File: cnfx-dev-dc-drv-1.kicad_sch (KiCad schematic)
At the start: 55 parts, among them J1 TC2030, J2 Conn_01x02, J3 Conn_01x04_Pin, J4 Conn_01x02, J7 Conn_01x03, J8 Conn_01x04_Pin, SW1 SW_Push, SW2 SW_Push, SW3 SW_Push, U1 SN65HVD230, U2 STM32F103C8Tx, U5 HT753-1, U6 TPS259472A, Y1 8M

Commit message: schem: run and fix ERC
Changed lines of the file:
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@@
 	)
 	(junction
+		(at 26.67 157.48)
+		(diameter 0)
+		(color 0 0 0 0)
+	)
+	(junction
 		(at 173.99 44.45)
 		(diameter 0)
@@
 	)
 	(junction
+		(at 25.4 153.67)
+		(diameter 0)
+		(color 0 0 0 0)
+	)
+	(junction
 		(at 62.23 124.46)
 		(diameter 0)
@@
 	(wire
 		(pts
-			(xy 24.13 153.67) (xy 27.94 153.67)
+			(xy 24.13 153.67) (xy 25.4 153.67)
 		)
 		(stroke
@@
 	(wire
 		(pts
+			(xy 25.4 153.67) (xy 27.94 153.67)
+		)
+		(stroke
+			(width 0)
+			(type default)
+		)
+	)
+	(wire
+		(pts
 			(xy 165.1 53.34) (xy 165.1 54.61)
 		)
@@
 	(wire
 		(pts
-			(xy 26.67 158.75) (xy 26.67 156.21)
+			(xy 26.67 158.75) (xy 26.67 157.48)
 		)
 		(stroke
@@
 	(wire
 		(pts
+			(xy 26.67 157.48) (xy 26.67 156.21)
+		)
+		(stroke
+			(width 0)
+			(type default)
+		)
+	)
+	(wire
+		(pts
 			(xy 35.56 166.37) (xy 36.83 166.37)
 		)
@@
 	)
 	(symbol
+		(lib_id "power:PWR_FLAG")
+		(at 26.67 157.48 270)
+		(unit 1)
+		(body_style 1)
+		(exclude_from_sim no)
+		(in_bom yes)
+		(on_board yes)
+		(in_pos_files yes)
+		(dnp no)
+		(fields_autoplaced yes)
+		(property "Reference" "#FLG02"
+			(at 28.575 157.48 0)
+			(hide yes)
+			(show_name no)
+			(do_not_autoplace no)
+			(effects
+				(font
+					(size 1.27 1.27)
+				)
+			)
+		)
+		(property "Value" "PWR_FLAG"
+			(at 31.75 157.48 0)
+			(hide yes)
+			(show_name no)
+			(do_not_autoplace no)
+			(effects
+				(font
+					(size 1.27 1.27)
+				)
+			)
+		)
+		(property "Footprint" ""
+			(at 26.67 157.48 0)
+			(hide yes)
+			(show_name no)
+			(do_not_autoplace no)
+			(effects
+				(font
+					(size 1.27 1.27)
+				)
+			)
+		)
+		(property "Datasheet" ""
+			(at 26.67 157.48 0)
+			(hide yes)
+			(show_name no)
+			(do_not_autoplace no)
+			(effects
+				(font
+					(size 1.27 1.27)
+				)
+			)
+		)
+		(property "Description" "Special symbol for telling ERC where power comes from"
+			(at 26.67 157.48 0)
+			(hide yes)
+			(show_name no)
+			(do_not_autoplace no)
+			(effects
+				(font
+					(size 1.27 1.27)
+				)
+			)
+		)
+		(pin "1"
+		)
+		(instances
+			(project "cnfx-dev-dc-drv-1"
+				(path "/d7250a19-615d-468e-abbc-0dea4b78aeef"
+					(reference "#FLG02")
+					(unit 1)
+				)
+			)
+		)
+	)
+	(symbol
 		(lib_id "power:GND")
 		(at 182.88 142.24 0)
@@
 					(unit 1)
 				)
+			)
+		)
+	)
+	(symbol
+		(lib_id "power:PWR_FLAG")
+		(at 25.4 153.67 0)
+		(unit 1)
+		(body_style 1)
+		(exclude_from_sim no)
+		(in_bom yes)
+		(on_board yes)
+		(in_pos_files yes)
+		(dnp no)
+		(fields_autoplaced yes)
+		(property "Reference" "#FLG01"
+			(at 25.4 151.765 0)
+			(hide yes)
+			(show_name no)
+			(do_not_autoplace no)
+			(effects
+				(font
+					(size 1.27 1.27)
+				)
+			)
+		)
+		(property "Value" "PWR_FLAG"
+			(at 25.4 148.59 0)
+			(hide yes)
+			(show_name no)
+			(do_not_autoplace no)
+			(effects
+				(font
+					(size 1.27 1.27)
+				)
+			)
+		)
+		(property "Footprint" ""
+			(at 25.4 153.67 0)
+			(hide yes)
+			(show_name no)
+			(do_not_autoplace no)
+			(effects
+				(font
+					(size 1.27 1.27)
+				)
+			)
+		)
+		(property "Datasheet" ""
+			(at 25.4 153.67 0)
+			(hide yes)
+			(show_name no)
+			(do_not_autoplace no)
+			(effects
+				(font
+					(size 1.27 1.27)
+				)
+			)
+		)
+		(property "Description" "Special symbol for telling ERC where power comes from"
+			(at 25.4 153.67 0)
+			(hide yes)
+			(show_name no)
+			(do_not_autoplace no)
+			(effects
+				(font
+					(size 1.27 1.27)
+				)
+			)
+		)
+		(pin "1"
+		)
+		(instances
+			(project "cnfx-dev-dc-drv-1"
+				(path "/d7250a19-615d-468e-abbc-0dea4b78aeef"
+					(reference "#FLG01")
+					(unit 1)
+				)

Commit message: schem: add title
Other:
- company: (none) -> Rémi Ait-Younes
- title: (none) -> CNFX DEV DC Driver 1
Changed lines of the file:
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@@
 	(generator_version "10.0")
 	(paper "A4")
+	(title_block
+		(title "CNFX DEV DC Driver 1")
+		(date "2026-04-11")
+		(rev "01")
+		(company "Rémi Ait-Younes")
+	)
 	(rectangle
 		(start 219.71 64.77)

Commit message: schem: reannotate
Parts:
- renumbered C10 to C1, C5 to C10, C6 to C11, C8 to C12, C9 to C13, C11 to C14, C12 to C15, C13 to C16, C14 to C17, C15 to C18, C1 to C2, C22 to C3, C23 to C4, C24 to C5, C2 to C6, C3 to C7, C7 to C8, C4 to C9, D3 to D2, D4 to D3, D5 to D4, D6 to D5, D8 to D6, D11 to D8, J7 to J1, J1 to J2, J2 to J3, J3 to J5, J8 to J6, R3 to R1, R5 to R2, R7 to R3, R9 to R4, R10 to R5, R4 to R6, R6 to R7, TP6 to TP1, TP7 to TP2, TP5 to TP4, TP4 to TP5, U6 to U2, U5 to U3, U2 to U4

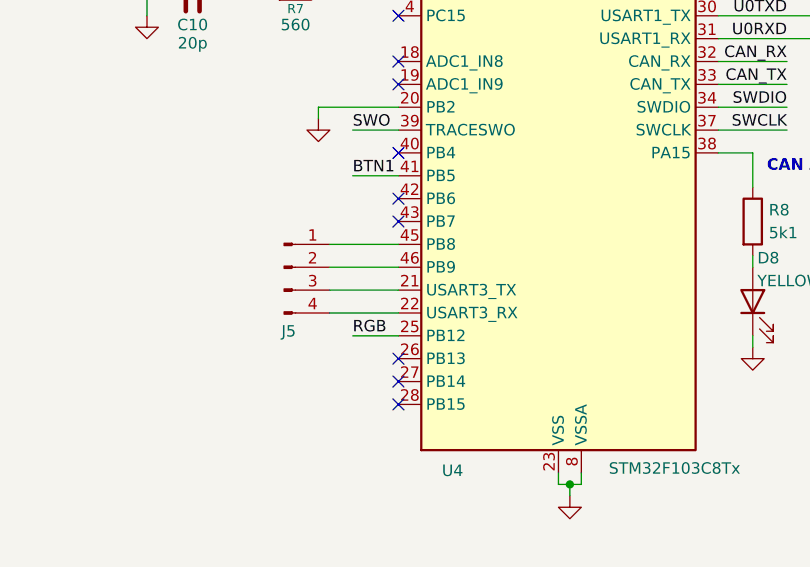
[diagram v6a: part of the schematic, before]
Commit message: schem: remove extra gpios
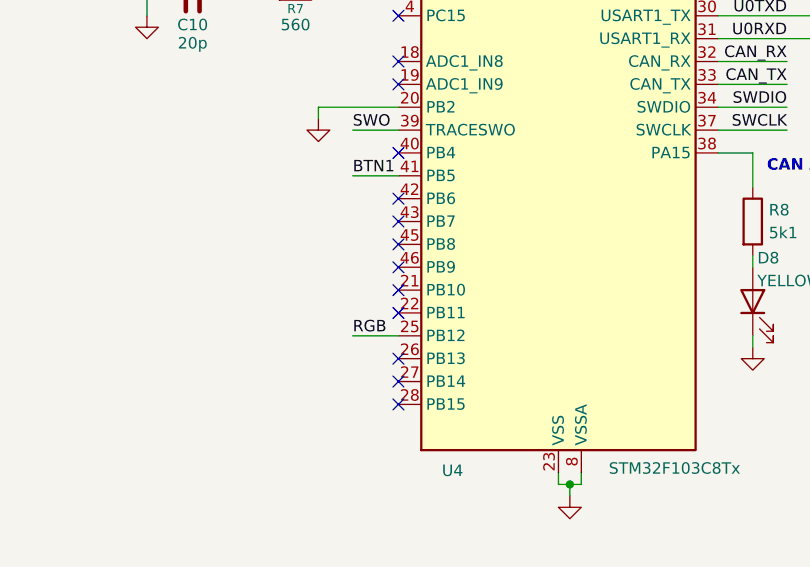
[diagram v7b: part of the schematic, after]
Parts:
- removed J5: Conn_01x04_Pin, Connector_PinHeader_2.54mm:PinHeader_1x04_P2.54mm_Vertical, symbol Connector:Conn_01x04_Pin
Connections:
- no-connect marks 18 -> 22
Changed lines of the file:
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@@
 	)
 	(no_connect
+		(at 163.83 121.92)
+	)
+	(no_connect
 		(at 163.83 83.82)
 	)
@@
 	)
 	(no_connect
+		(at 163.83 116.84)
+	)
+	(no_connect
 		(at 199.39 73.66)
 	)
@@
 	)
 	(no_connect
+		(at 163.83 114.3)
+	)
+	(no_connect
 		(at 199.39 76.2)
 	)
 	(no_connect
+		(at 163.83 119.38)
+	)
+	(no_connect
 		(at 163.83 109.22)
 	)
@@
 	(wire
 		(pts
-			(xy 163.83 119.38) (xy 156.21 119.38)
-		)
-		(stroke
-			(width 0)
-			(type default)
-		)
-	)
-	(wire
-		(pts
 			(xy 55.88 99.06) (xy 55.88 97.79)
 		)
@@
 	(wire
 		(pts
-			(xy 163.83 121.92) (xy 156.21 121.92)
-		)
-		(stroke
-			(width 0)
-			(type default)
-		)
-	)
-	(wire
-		(pts
 			(xy 48.26 127) (xy 55.88 127)
 		)
@@
 	(wire
 		(pts
-			(xy 163.83 114.3) (xy 156.21 114.3)
-		)
-		(stroke
-			(width 0)
-			(type default)
-		)
-	)
-	(wire
-		(pts
 			(xy 60.96 187.96) (xy 60.96 189.23)
 		)
@@
 	(wire
 		(pts
-			(xy 163.83 116.84) (xy 156.21 116.84)
-		)
-		(stroke
-			(width 0)
-			(type default)
-		)
-	)
-	(wire
-		(pts
 			(xy 203.2 124.46) (xy 203.2 125.73)
 		)
@@
 		)
 		(pin "22"
-			(alternate "USART3_RX")
 		)
 		(pin "29"
@@
 		)
 		(pin "21"
-			(alternate "USART3_TX")
 		)
 		(pin "27"
@@
 					(unit 1)
 				)
-			)
-		)
-	)
-	(symbol
-		(lib_id "Connector:Conn_01x04_Pin")
-		(at 151.13 116.84 0)
-		(unit 1)
-		(body_style 1)
-		(exclude_from_sim no)
-		(in_bom no)
-		(on_board yes)
-		(in_pos_files yes)
-		(dnp no)
-		(property "Reference" "J5"
-			(at 151.638 123.952 0)
-			(show_name no)
-			(do_not_autoplace no)
-			(effects
-				(font
-					(size 1.27 1.27)
-				)
-			)
-		)
-		(property "Value" "Conn_01x04_Pin"
-			(at 148.59 118.11 90)
-			(hide yes)
-			(show_name no)
-			(do_not_autoplace no)
-			(effects
-				(font
-					(size 1.27 1.27)
-				)
-			)
-		)
-		(property "Footprint" "Connector_PinHeader_2.54mm:PinHeader_1x04_P2.54mm_Vertical"
-			(at 151.13 116.84 0)
-			(hide yes)
-			(show_name no)
-			(do_not_autoplace no)
-			(effects
-				(font
-					(size 1.27 1.27)
-				)
-			)
-		)
-		(property "Datasheet" ""
-			(at 151.13 116.84 0)
-			(hide yes)
-			(show_name no)
-			(do_not_autoplace no)
-			(effects
-				(font
-					(size 1.27 1.27)
-				)
-			)
-		)
-		(property "Description" "Generic connector, single row, 01x04, script generated"
-			(at 151.13 116.84 0)
-			(hide yes)
-			(show_name no)
-			(do_not_autoplace no)
-			(effects
-				(font
-					(size 1.27 1.27)
-				)
-			)
-		)
-		(pin "4"
-		)
-		(pin "3"
-		)
-		(pin "2"
-		)
-		(pin "1"
-		)
-		(instances
-			(project "cnfx-dev-dc-drv-1"
-				(path "/d7250a19-615d-468e-abbc-0dea4b78aeef"
-					(reference "J5")
-					(unit 1)
-				)

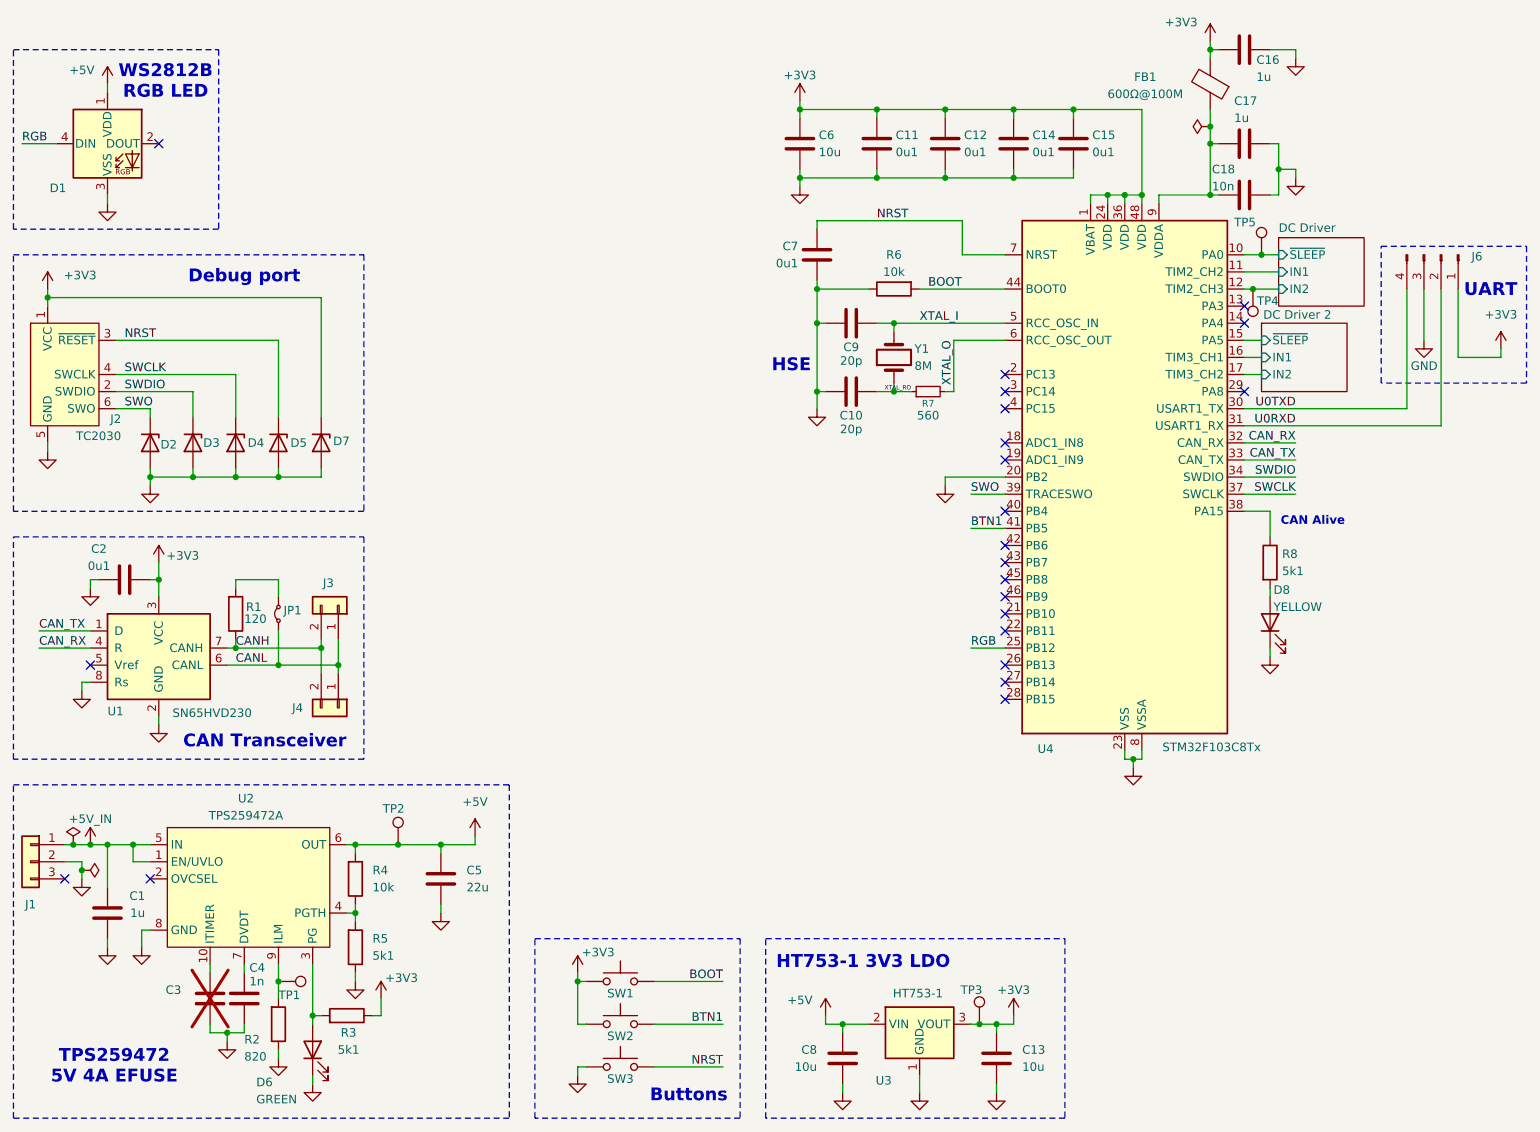
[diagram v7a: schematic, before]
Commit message: schem: add ILM efuse reading to stm32
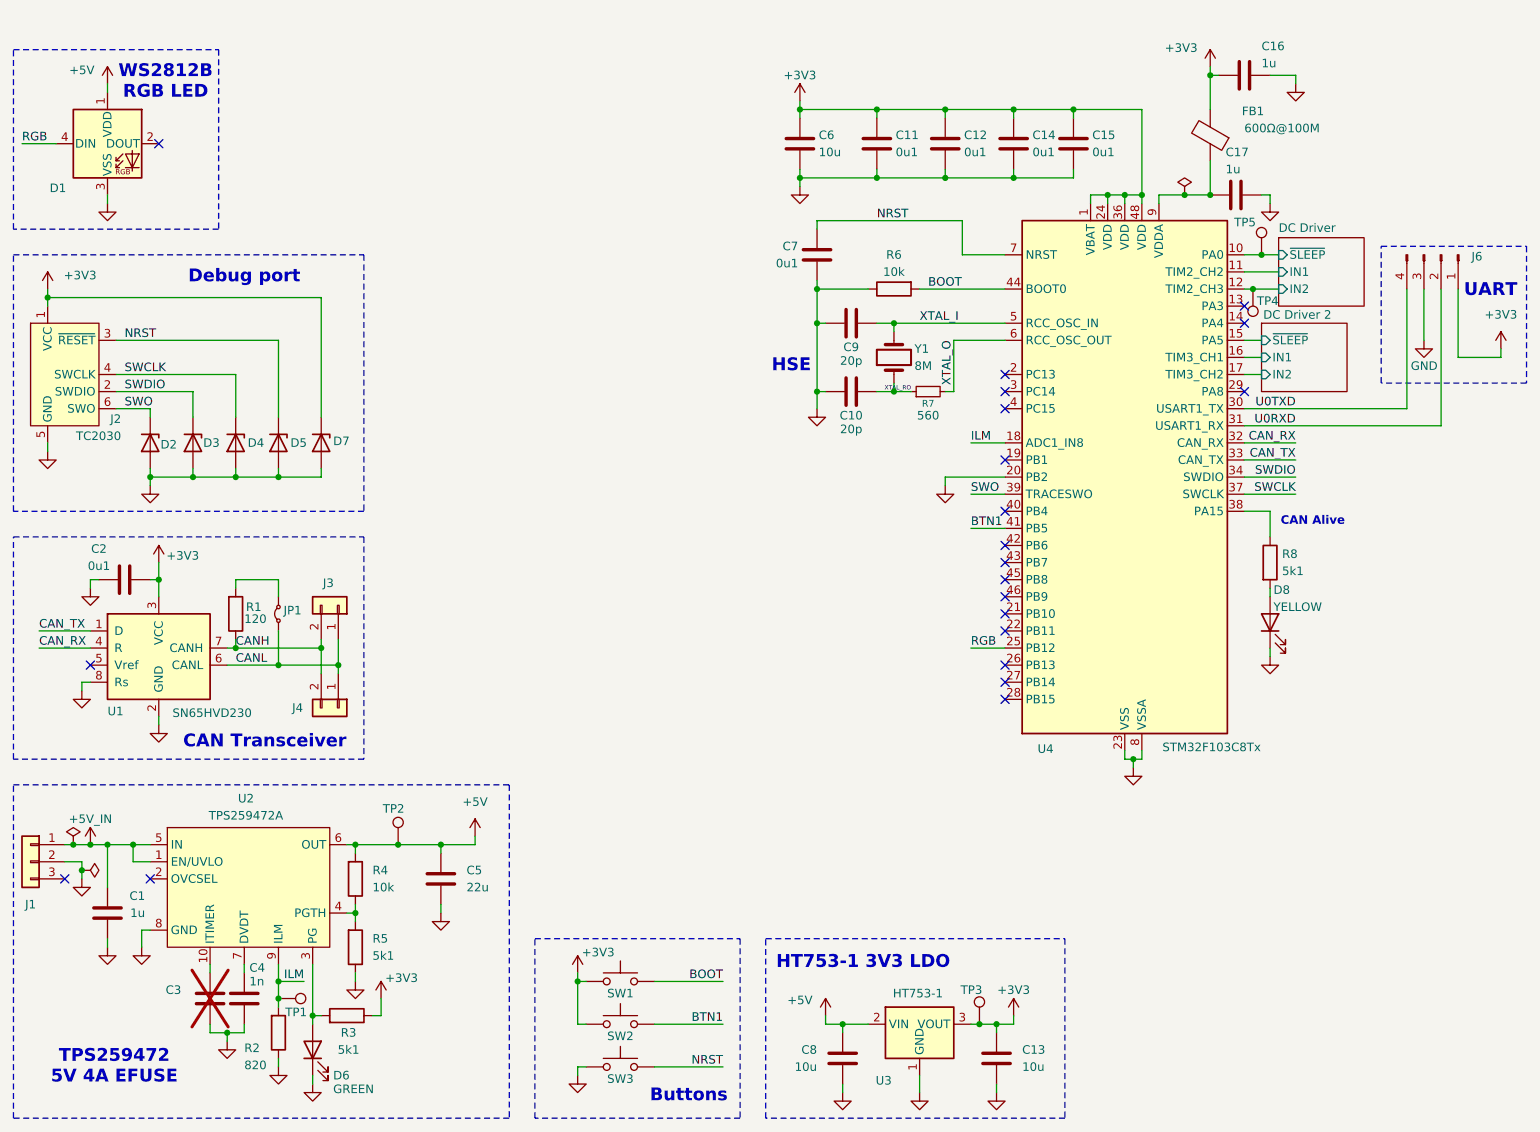
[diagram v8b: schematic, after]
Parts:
- removed C18: 10n, Capacitor_SMD:C_0402_1005Metric, symbol Device:C
- JP1: footprint Jumper:SolderJumper-2_P1.3mm_Open_RoundedPad1.0x1.5mm -> Connector_PinHeader_2.54mm:PinHeader_1x02_P2.54mm_Vertical
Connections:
- net ILM: now reaches R2.2, TP1.1, U2.9 (ILM)
- net ILM: now also U4.18 (PB0)
- no-connect marks 22 -> 21
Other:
- moved on the sheet: C16, C17, FB1, R2, TP1
